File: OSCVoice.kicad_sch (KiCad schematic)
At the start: 39 parts, among them U15 4066, U16 TL072, U22 SSI2131, U5 MCP6004, U8 4066

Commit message: Added readme
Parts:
- U15, U8: value 4066 -> 74LV4066PW
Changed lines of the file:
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@@
     (in_bom yes) (on_board yes) (fields_autoplaced)
     (property "Reference" "U15" (id 0) (at 205.74 60.96 0))
-    (property "Value" "4066" (id 1) (at 205.74 63.5 0))
+    (property "Value" "74LV4066PW" (id 1) (at 205.74 63.5 0))
     (property "Footprint" "Package_SO:TSSOP-14_4.4x5mm_P0.65mm" (id 2) (at 205.74 55.88 0)
       (effects (font (size 1.27 1.27)) hide)
     )
-    (property "Datasheet" "http://www.ti.com/lit/ds/symlink/cd4066b.pdf" (id 3) (at 205.74 55.88 0)
+    (property "Datasheet" "https://www.nexperia.com/products/analog-logic-ics/i-o-expansion-logic/analog-switches/74LV4066PW.html" (id 3) (at 205.74 55.88 0)
       (effects (font (size 1.27 1.27)) hide)
     )
@@
     (in_bom yes) (on_board yes) (fields_autoplaced)
     (property "Reference" "U15" (id 0) (at 205.74 36.83 0))
-    (property "Value" "4066" (id 1) (at 205.74 39.37 0))
+    (property "Value" "74LV4066PW" (id 1) (at 205.74 39.37 0))
     (property "Footprint" "Package_SO:TSSOP-14_4.4x5mm_P0.65mm" (id 2) (at 205.74 31.75 0)
       (effects (font (size 1.27 1.27)) hide)
     )
-    (property "Datasheet" "http://www.ti.com/lit/ds/symlink/cd4066b.pdf" (id 3) (at 205.74 31.75 0)
+    (property "Datasheet" "https://www.nexperia.com/products/analog-logic-ics/i-o-expansion-logic/analog-switches/74LV4066PW.html" (id 3) (at 205.74 31.75 0)
       (effects (font (size 1.27 1.27)) hide)
     )
@@
       (effects (font (size 1.27 1.27)) (justify left))
     )
-    (property "Value" "4066" (id 1) (at 251.46 137.1599 0)
+    (property "Value" "74LV4066PW" (id 1) (at 251.46 137.1599 0)
       (effects (font (size 1.27 1.27)) (justify left))
     )
@@
       (effects (font (size 1.27 1.27)) hide)
     )
-    (property "Datasheet" "http://www.ti.com/lit/ds/symlink/cd4066b.pdf" (id 3) (at 245.11 135.89 0)
+    (property "Datasheet" "https://www.nexperia.com/products/analog-logic-ics/i-o-expansion-logic/analog-switches/74LV4066PW.html" (id 3) (at 245.11 135.89 0)
       (effects (font (size 1.27 1.27)) hide)
     )
@@
     (in_bom yes) (on_board yes) (fields_autoplaced)
     (property "Reference" "U15" (id 0) (at 259.08 36.83 0))
-    (property "Value" "4066" (id 1) (at 259.08 39.37 0))
+    (property "Value" "74LV4066PW" (id 1) (at 259.08 39.37 0))
     (property "Footprint" "Package_SO:TSSOP-14_4.4x5mm_P0.65mm" (id 2) (at 259.08 31.75 0)
       (effects (font (size 1.27 1.27)) hide)
     )
-    (property "Datasheet" "http://www.ti.com/lit/ds/symlink/cd4066b.pdf" (id 3) (at 259.08 31.75 0)
+    (property "Datasheet" "https://www.nexperia.com/products/analog-logic-ics/i-o-expansion-logic/analog-switches/74LV4066PW.html" (id 3) (at 259.08 31.75 0)
       (effects (font (size 1.27 1.27)) hide)
     )
@@
     (in_bom yes) (on_board yes) (fields_autoplaced)
     (property "Reference" "U15" (id 0) (at 205.74 83.82 0))
-    (property "Value" "4066" (id 1) (at 205.74 86.36 0))
+    (property "Value" "74LV4066PW" (id 1) (at 205.74 86.36 0))
     (property "Footprint" "Package_SO:TSSOP-14_4.4x5mm_P0.65mm" (id 2) (at 205.74 78.74 0)
       (effects (font (size 1.27 1.27)) hide)
     )
-    (property "Datasheet" "http://www.ti.com/lit/ds/symlink/cd4066b.pdf" (id 3) (at 205.74 78.74 0)
+    (property "Datasheet" "https://www.nexperia.com/products/analog-logic-ics/i-o-expansion-logic/analog-switches/74LV4066PW.html" (id 3) (at 205.74 78.74 0)
       (effects (font (size 1.27 1.27)) hide)
     )
@@
     (in_bom yes) (on_board yes) (fields_autoplaced)
     (property "Reference" "U8" (id 0) (at 259.08 60.96 0))
-    (property "Value" "4066" (id 1) (at 259.08 63.5 0))
+    (property "Value" "74LV4066PW" (id 1) (at 259.08 63.5 0))
     (property "Footprint" "Package_SO:TSSOP-14_4.4x5mm_P0.65mm" (id 2) (at 259.08 55.88 0)
       (effects (font (size 1.27 1.27)) hide)
     )
-    (property "Datasheet" "http://www.ti.com/lit/ds/symlink/cd4066b.pdf" (id 3) (at 259.08 55.88 0)
-      (effects (font (size 1.27 1.27)) hide)
-    )
+    (property "Datasheet" "https://www.nexperia.com/products/analog-logic-ics/i-o-expansion-logic/analog-switches/74LV4066PW.html" (id 3) (at 259.08 55.88 0)
+      (effects (font (size 1.27 1.27)) hide)
+    )

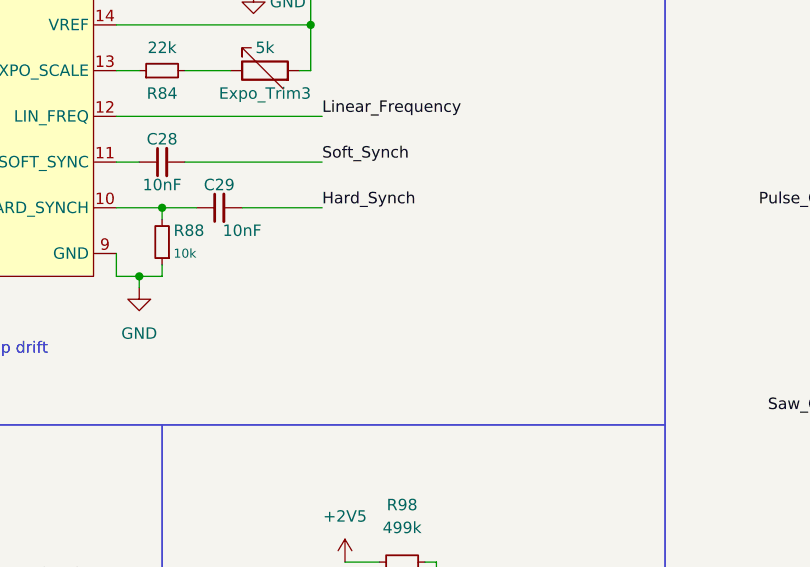
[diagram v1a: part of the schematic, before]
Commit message: v2.0 Update with Synch pulse at start to fix oscillators not starting
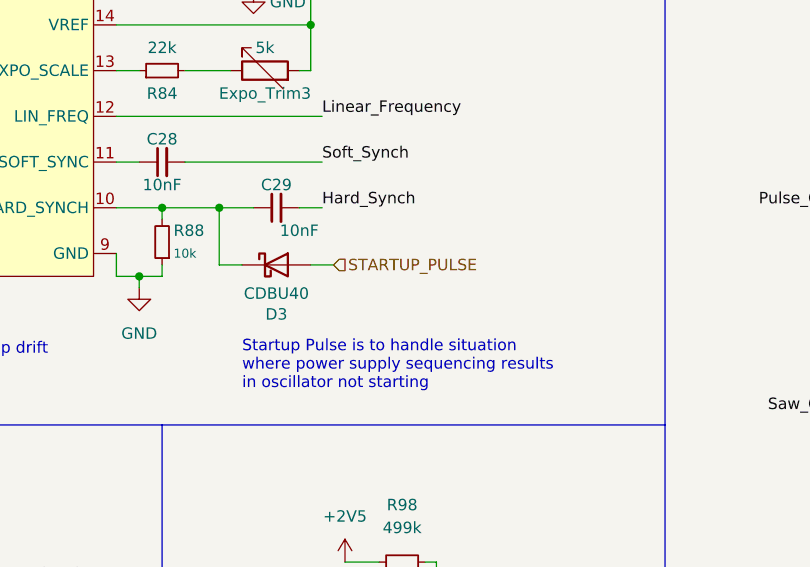
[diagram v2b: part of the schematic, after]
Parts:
- added D3: CDBU40, Diode_SMD:D_0603_1608Metric, symbol Diode:1N5819
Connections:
- net at C29.1, R88.2, U22.10 (HARD_SYNCH): now also D3.1 (K)
- new net STARTUP_PULSE: D3.2 (A)
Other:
- note added: "Startup Pulse is to handle situation where power supply sequencing results in oscillator not starting"
- moved on the sheet: C29
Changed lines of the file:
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@@
   (junction (at 60.96 147.32) (diameter 0) (color 0 0 0 0)
   )
+  (junction (at 127 55.88) (diameter 0) (color 0 0 0 0)
+  )
   (junction (at 160.02 160.02) (diameter 0) (color 0 0 0 0)
   )
@@
     (stroke (width 0) (type default) (color 0 0 0 0))
   )
-  (wire (pts (xy 129.54 55.88) (xy 138.43 55.88))
+  (wire (pts (xy 135.89 55.88) (xy 138.43 55.88))
     (stroke (width 0) (type default) (color 0 0 0 0))
   )
@@
     (stroke (width 0) (type default) (color 0 0 0 0))
   )
+  (wire (pts (xy 127 55.88) (xy 130.81 55.88))
+    (stroke (width 0) (type default) (color 0 0 0 0))
+  )
   (wire (pts (xy 245.11 120.65) (xy 245.11 123.19))
     (stroke (width 0) (type default) (color 0 0 0 0))
@@
     (stroke (width 0) (type default) (color 0 0 0 0))
   )
+  (wire (pts (xy 127 55.88) (xy 127 62.23))
+    (stroke (width 0) (type default) (color 0 0 0 0))
+  )
   (wire (pts (xy 203.2 127) (xy 205.74 127))
     (stroke (width 0) (type default) (color 0 0 0 0))
@@
     (stroke (width 0) (type default) (color 0 0 0 0))
   )
+  (wire (pts (xy 127 62.23) (xy 129.54 62.23))
+    (stroke (width 0) (type default) (color 0 0 0 0))
+  )
   (wire (pts (xy 80.01 45.72) (xy 82.55 45.72))
     (stroke (width 0) (type default) (color 0 0 0 0))
@@
     (stroke (width 0) (type default) (color 0 0 0 0))
   )
+  (wire (pts (xy 137.16 62.23) (xy 139.7 62.23))
+    (stroke (width 0) (type default) (color 0 0 0 0))
+  )
   (wire (pts (xy 64.77 62.23) (xy 64.77 63.5))
     (stroke (width 0) (type default) (color 0 0 0 0))
@@
     (stroke (width 0) (type default) (color 0 0 0 0))
   )
-  (wire (pts (xy 120.65 55.88) (xy 124.46 55.88))
+  (wire (pts (xy 120.65 55.88) (xy 127 55.88))
     (stroke (width 0) (type default) (color 0 0 0 0))
   )
@@
     (effects (font (size 1.27 1.27)) (justify left bottom))
   )
+  (text "Startup Pulse is to handle situation \nwhere power supply sequencing results \nin oscillator not starting\n"
+    (at 129.54 76.2 0)
+    (effects (font (size 1.27 1.27)) (justify left bottom))
+  )
   (text "Fine tune resistor value TBA" (at 29.21 20.32 0)
     (effects (font (size 1.27 1.27)) (justify left bottom))
@@
   (hierarchical_label "LIN_FREQ" (shape input) (at 140.97 100.33 180)
     (effects (font (size 1.27 1.27)) (justify right))
+  )
+  (hierarchical_label "STARTUP_PULSE" (shape input) (at 139.7 62.23 0)
+    (effects (font (size 1.27 1.27)) (justify left))
   )
   (hierarchical_label "OCTAVE_TUNE" (shape input) (at 49.53 50.8 180)
@@
     (pin "1")
   )
-  (symbol (lib_id "Device:C_Small") (at 127 55.88 90) (unit 1)
-    (in_bom yes) (on_board yes)
-    (property "Reference" "C29" (id 0) (at 127 53.34 90))
-    (property "Value" "10nF" (id 1) (at 129.54 58.42 90))
-    (property "Footprint" "Capacitor_SMD:C_0603_1608Metric_Pad1.08x0.95mm_HandSolder" (id 2) (at 127 55.88 0)
-      (effects (font (size 1.27 1.27)) hide)
-    )
-    (property "Datasheet" "~" (id 3) (at 127 55.88 0)
+  (symbol (lib_id "Device:C_Small") (at 133.35 55.88 90) (unit 1)
+    (in_bom yes) (on_board yes)
+    (property "Reference" "C29" (id 0) (at 133.35 53.34 90))
+    (property "Value" "10nF" (id 1) (at 135.89 58.42 90))
+    (property "Footprint" "Capacitor_SMD:C_0603_1608Metric_Pad1.08x0.95mm_HandSolder" (id 2) (at 133.35 55.88 0)
+      (effects (font (size 1.27 1.27)) hide)
+    )
+    (property "Datasheet" "~" (id 3) (at 133.35 55.88 0)
       (effects (font (size 1.27 1.27)) hide)
     )
@@
     (pin "2")
   )
+  (symbol (lib_id "Diode:1N5819") (at 133.35 62.23 0) (unit 1)
+    (in_bom yes) (on_board yes)
+    (property "Reference" "D3" (id 0) (at 133.35 67.7164 0))
+    (property "Value" "CDBU40" (id 1) (at 133.35 65.405 0))
+    (property "Footprint" "Diode_SMD:D_0603_1608Metric" (id 2) (at 133.35 66.675 0)
+      (effects (font (size 1.27 1.27)) hide)
+    )
+    (property "Datasheet" "http://www.vishay.com/docs/88525/1n5817.pdf" (id 3) (at 133.35 62.23 0)
+      (effects (font (size 1.27 1.27)) hide)
+    )
+    (property "Part_Number" "C8598" (id 4) (at 133.35 62.23 0)
+      (effects (font (size 1.27 1.27)) hide)
+    )
+    (pin "1")
+    (pin "2")
+  )
   (symbol (lib_id "Device:C_Small") (at 250.19 123.19 90) (unit 1)
     (in_bom yes) (on_board yes)
@@
       (effects (font (size 1.27 1.27)) hide)
     )
-    (property "Datasheet" "https://www.nexperia.com/products/analog-logic-ics/i-o-expansion-logic/analog-switches/74LV4066PW.html" (id 3) (at 205.74 55.88 0)
+    (property "Datasheet" "http://www.ti.com/lit/ds/symlink/cd4066b.pdf" (id 3) (at 205.74 55.88 0)
       (effects (font (size 1.27 1.27)) hide)
     )
@@
       (effects (font (size 1.27 1.27)) hide)
     )
-    (property "Datasheet" "https://www.nexperia.com/products/analog-logic-ics/i-o-expansion-logic/analog-switches/74LV4066PW.html" (id 3) (at 205.74 31.75 0)
+    (property "Datasheet" "http://www.ti.com/lit/ds/symlink/cd4066b.pdf" (id 3) (at 205.74 31.75 0)
       (effects (font (size 1.27 1.27)) hide)
     )
@@
       (effects (font (size 1.27 1.27)) hide)
     )
-    (property "Datasheet" "https://www.nexperia.com/products/analog-logic-ics/i-o-expansion-logic/analog-switches/74LV4066PW.html" (id 3) (at 245.11 135.89 0)
+    (property "Datasheet" "http://www.ti.com/lit/ds/symlink/cd4066b.pdf" (id 3) (at 245.11 135.89 0)
       (effects (font (size 1.27 1.27)) hide)
     )
@@
       (effects (font (size 1.27 1.27)) hide)
     )
-    (property "Datasheet" "https://www.nexperia.com/products/analog-logic-ics/i-o-expansion-logic/analog-switches/74LV4066PW.html" (id 3) (at 259.08 31.75 0)
+    (property "Datasheet" "http://www.ti.com/lit/ds/symlink/cd4066b.pdf" (id 3) (at 259.08 31.75 0)
       (effects (font (size 1.27 1.27)) hide)
     )
@@
       (effects (font (size 1.27 1.27)) hide)
     )
-    (property "Datasheet" "https://www.nexperia.com/products/analog-logic-ics/i-o-expansion-logic/analog-switches/74LV4066PW.html" (id 3) (at 205.74 78.74 0)
+    (property "Datasheet" "http://www.ti.com/lit/ds/symlink/cd4066b.pdf" (id 3) (at 205.74 78.74 0)
       (effects (font (size 1.27 1.27)) hide)
     )
@@
       (effects (font (size 1.27 1.27)) hide)
     )
-    (property "Datasheet" "https://www.nexperia.com/products/analog-logic-ics/i-o-expansion-logic/analog-switches/74LV4066PW.html" (id 3) (at 259.08 55.88 0)
-      (effects (font (size 1.27 1.27)) hide)
-    )
+    (property "Datasheet" "http://www.ti.com/lit/ds/symlink/cd4066b.pdf" (id 3) (at 259.08 55.88 0)
+      (effects (font (size 1.27 1.27)) hide)
+    )

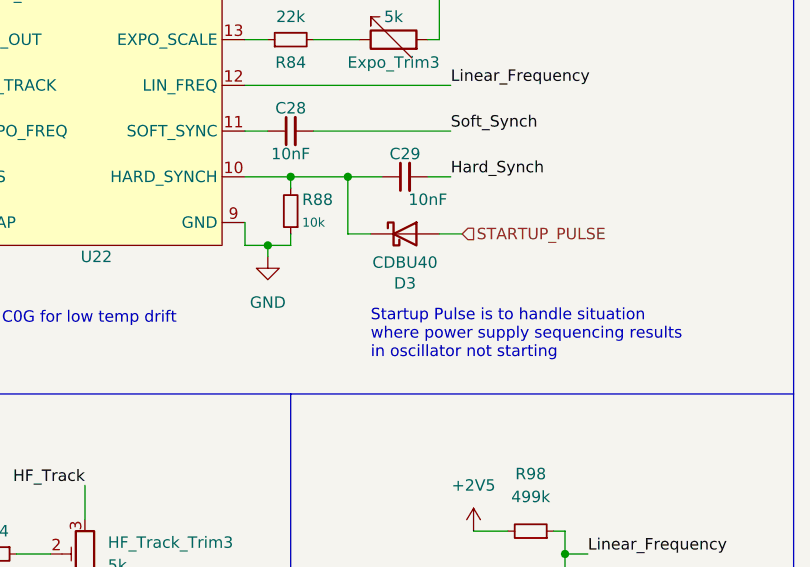
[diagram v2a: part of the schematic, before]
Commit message: Updated production files for version 2 (Start up pulse)
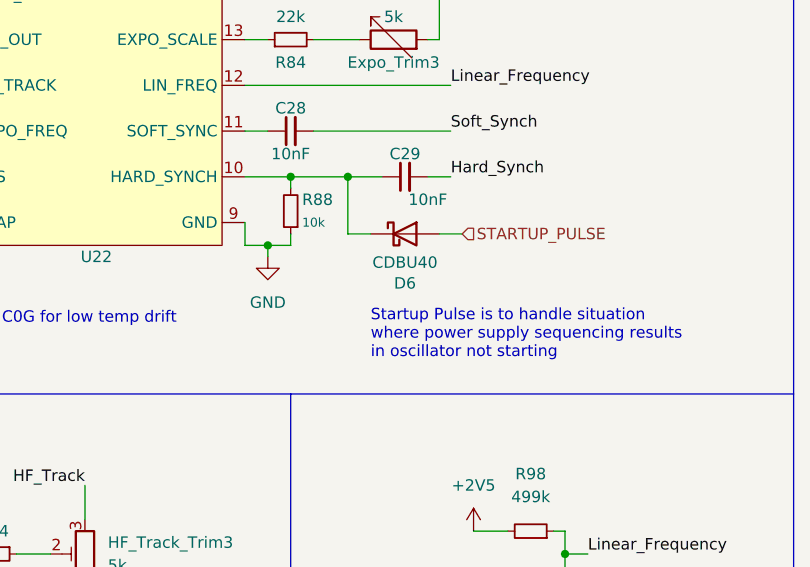
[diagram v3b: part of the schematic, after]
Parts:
- renumbered D3 to D6
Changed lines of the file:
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@@
   (symbol (lib_id "Diode:1N5819") (at 133.35 62.23 0) (unit 1)
     (in_bom yes) (on_board yes)
-    (property "Reference" "D3" (id 0) (at 133.35 67.7164 0))
+    (property "Reference" "D6" (id 0) (at 133.35 67.7164 0))
     (property "Value" "CDBU40" (id 1) (at 133.35 65.405 0))
     (property "Footprint" "Diode_SMD:D_0603_1608Metric" (id 2) (at 133.35 66.675 0)

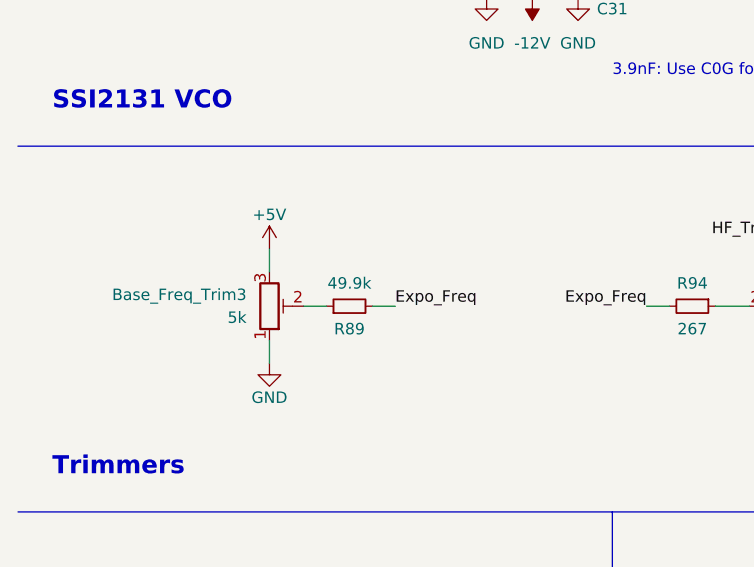
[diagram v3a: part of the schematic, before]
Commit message: Added alternative control pcb layout with 3 way switch for octave
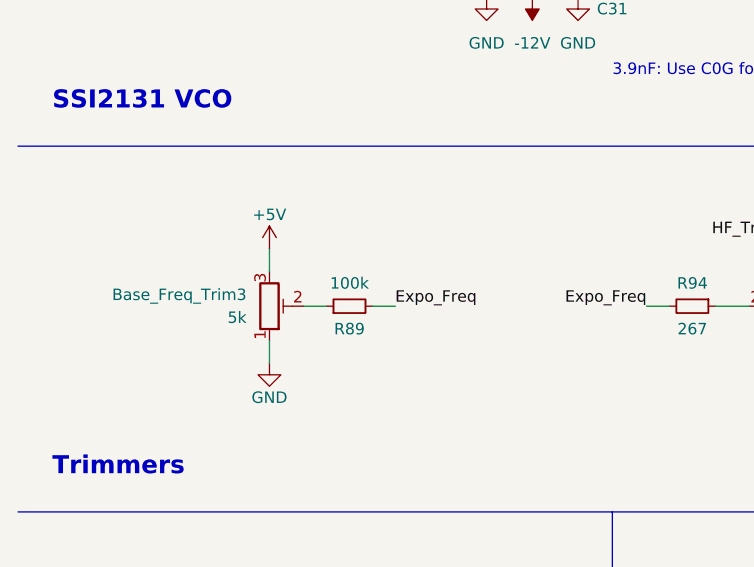
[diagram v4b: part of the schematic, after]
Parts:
- R89: value 49.9k -> 100k
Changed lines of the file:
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@@
     (in_bom yes) (on_board yes)
     (property "Reference" "R89" (id 0) (at 49.53 100.33 90))
-    (property "Value" "49.9k" (id 1) (at 49.53 95.25 90))
+    (property "Value" "100k" (id 1) (at 49.53 95.25 90))
     (property "Footprint" "Resistor_SMD:R_0603_1608Metric" (id 2) (at 49.53 97.79 0)
       (effects (font (size 1.27 1.27)) hide)

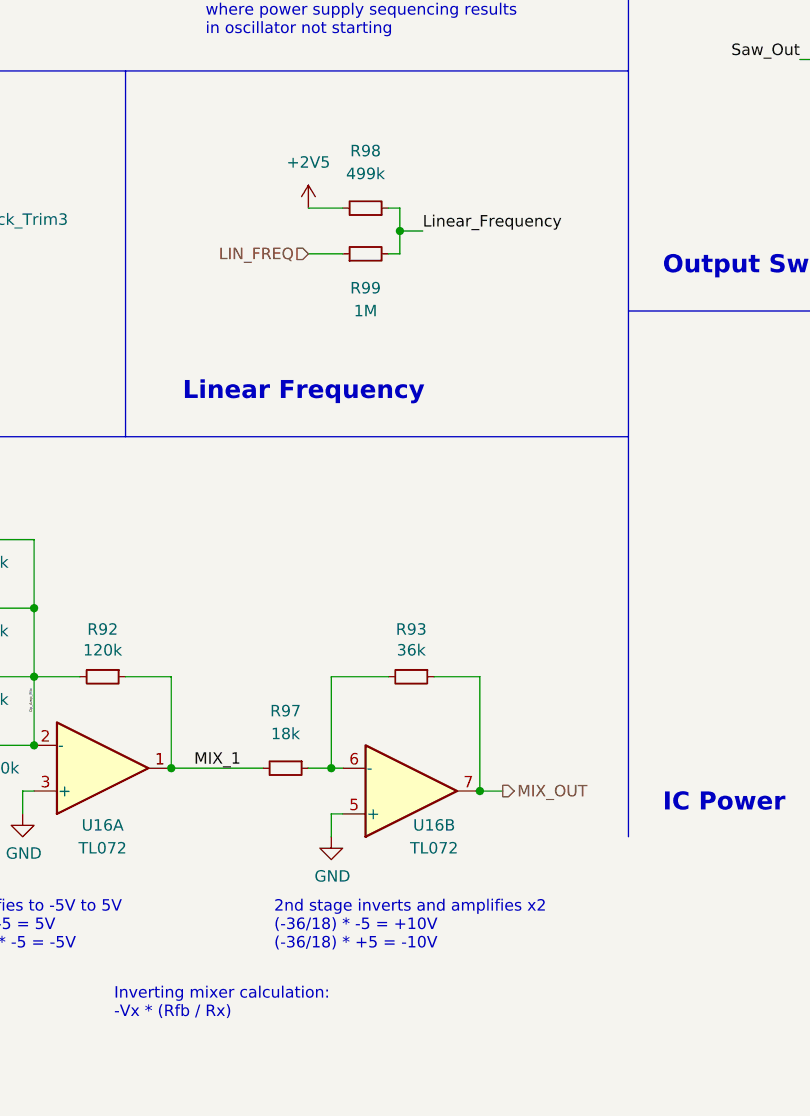
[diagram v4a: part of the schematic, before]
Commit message: Updates to v3; changed output mix feedback resistors to lower output level
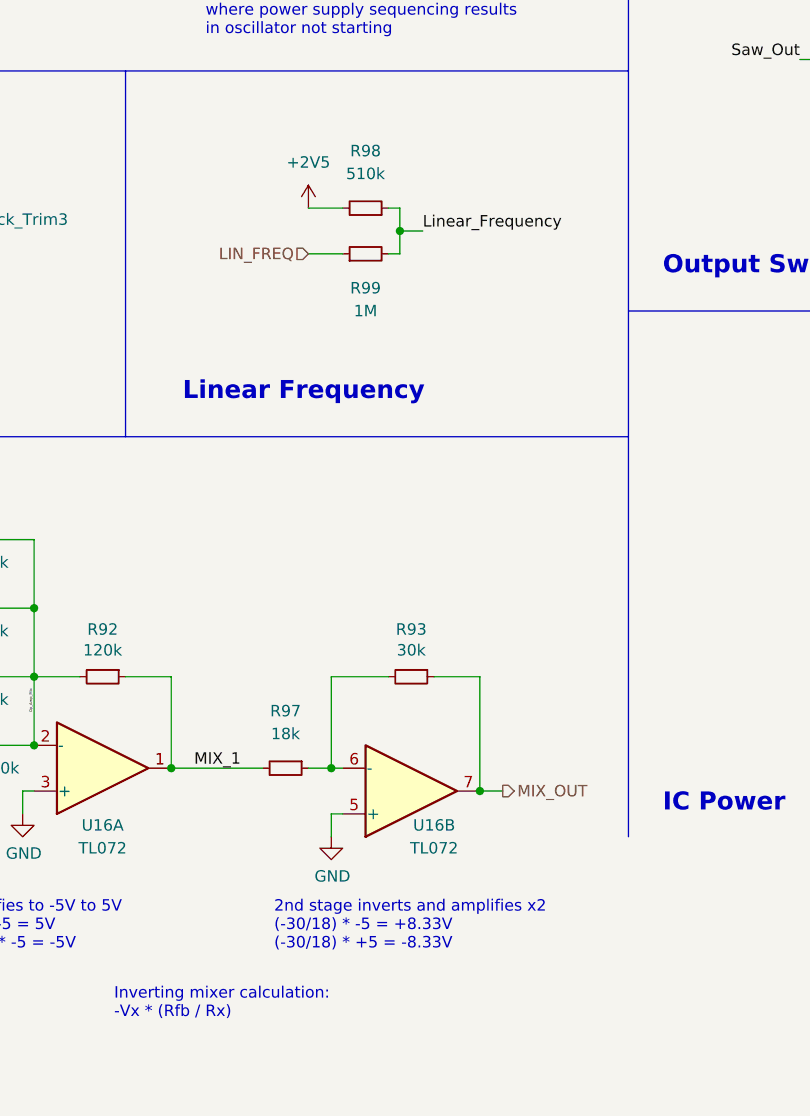
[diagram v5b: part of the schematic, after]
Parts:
- R93: value 36k -> 30k
- R98: value 499k -> 510k
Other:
- note added: "2nd stage inverts and amplifies x2 (-30/18) * -5 = +8.33V (-30/18) * +5 = -8.33V"
- note removed: "2nd stage inverts and amplifies x2 (-36/18) * -5 = +10V (-36/18) * +5 = -10V"
